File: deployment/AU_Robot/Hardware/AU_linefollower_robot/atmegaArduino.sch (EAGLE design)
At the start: 11 parts

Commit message: updated arduino sw
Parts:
- added LED1, LED2, LED3: (no value), eagle-ltspice:LED_ELD260
- added R1, R2, R3: 270, rcl:R-EU_0204/5
- C1: device rcl:CPOL-EUE1.8-4 -> rcl:C-EU050-025X075
- JTAG: value (none) -> 2510-; device con-ml:ML10L -> con-3m:2510-
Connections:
- new net N$14: LED2.C, R2.2
- new net N$15: IC1.RESET, JTAG-6.KL
- new net N$16: LED3.C, R1.2
- new net N$17: IC1.OC2B/ICP/PCINT30, LED1.A
- new net N$18: IC1.OC1A/PCINT29, LED2.A
- new net N$19: IC1.XCK1/OC1B/PCINT28, LED3.A
- new net N$20: IC1.RXD1/INT0/PCINT26, IOH.2
- new net N$21: IC1.TXD1/INT1/PCINT27, IOH.1
- net GND: now also C1.2, JTAG-10.KL, JTAG-2.KL, R1.1, R2.1, R3.1; no longer C1.-, JTAG.10, JTAG.2
- net N$1: now also IC1.T3/RXD0/PCINT24; no longer IC1.TXD0/PCINT25
- net N$11: now also LED1.C, R3.2; no longer IC1.RESET, JTAG.6
- net N$2: now also IC1.TXD0/PCINT25; no longer IC1.T3/RXD0/PCINT24
- net N$3: now also JTAG-1.KL; no longer JTAG.1
- net N$4: now also IC1.TMS/PCINT19, JTAG-5.KL; no longer IC1.TDO/PCINT20, JTAG.3
- net N$6: now also IC1.TDO/PCINT20, JTAG-3.KL; no longer IC1.TDI/PCINT21, JTAG.9
- net N$8: now also IC1.TDI/PCINT21, JTAG-9.KL; no longer IC1.TMS/PCINT19, JTAG.5
- net VCC: now also C1.1, IC1.VCC, JTAG-4.KL; no longer C1.+, JTAG.4
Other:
- moved on the sheet: IOH, IOL, SERVO-LEFT, SERVO-RIGHT

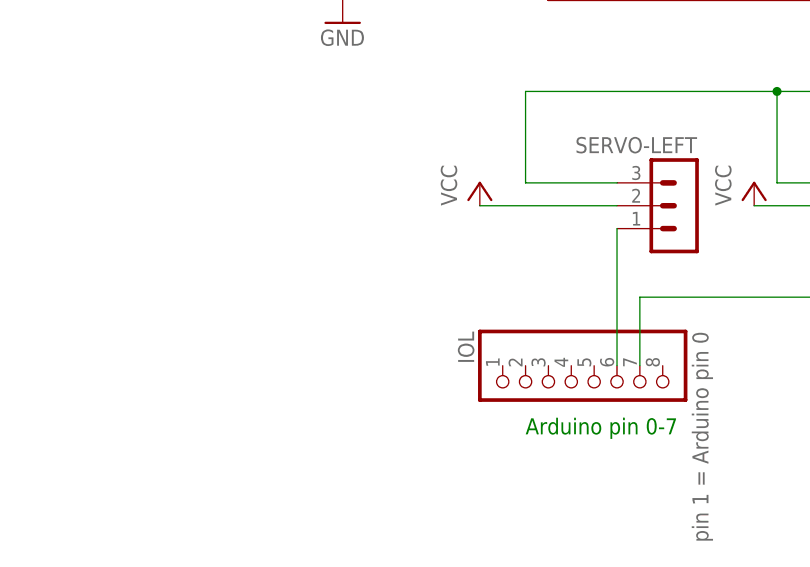
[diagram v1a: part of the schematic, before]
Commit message: updated schematics
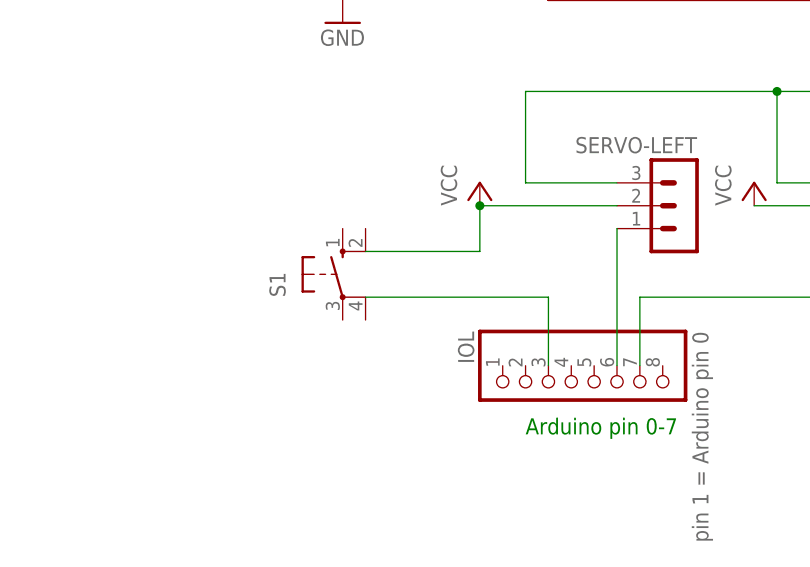
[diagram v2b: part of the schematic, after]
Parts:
- added S1: (no value), switch-omron:10-XX
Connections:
- new net N$22: IOL.3
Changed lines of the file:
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@@
 <part name="R2" library="rcl" deviceset="R-EU_" device="0204/5" value="270"/>
 <part name="R3" library="rcl" deviceset="R-EU_" device="0204/5" value="270"/>
+<part name="S1" library="switch-omron" deviceset="10-XX" device=""/>
 </parts>
 <sheets>
@@
 <instance part="R2" gate="G$1" x="157.48" y="-22.86" rot="R90"/>
 <instance part="R3" gate="G$1" x="147.32" y="-22.86" rot="R90"/>
+<instance part="S1" gate="1" x="48.26" y="-35.56"/>
 </instances>
 <busses>
@@
 <pinref part="P+4" gate="VCC" pin="VCC"/>
 <wire x1="78.74" y1="-27.94" x2="63.5" y2="-27.94" width="0.1524" layer="91"/>
+<wire x1="50.8" y1="-33.02" x2="63.5" y2="-33.02" width="0.1524" layer="91"/>
+<wire x1="63.5" y1="-33.02" x2="63.5" y2="-27.94" width="0.1524" layer="91"/>
+<junction x="63.5" y="-27.94"/>
 </segment>
 <segment>
@@
 </segment>
 </net>
+<net name="N$22" class="0">
+<segment>
+<pinref part="IOL" gate="A" pin="3"/>
+<wire x1="71.12" y1="-45.72" x2="71.12" y2="-38.1" width="0.1524" layer="91"/>
+<wire x1="71.12" y1="-38.1" x2="50.8" y2="-38.1" width="0.1524" layer="91"/>
+</segment>
+</net>
